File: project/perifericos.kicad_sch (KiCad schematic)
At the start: 67 parts, among them P1 Conector 2x10, P2 Conector 2x10, P3 Conector 2x10, P4 Conector 2x10, SW1 SW_Push, SW2 SW_Push, SW3 SW_Push, SW4 SW_Push, SW5 SW_Push, SW6 SW_Push, SW7 SW_Push, SW8 SW_Push, U6 ICE40HX4K-TQ144, Y2 ECS-3225MVQ-1000-CN-TR

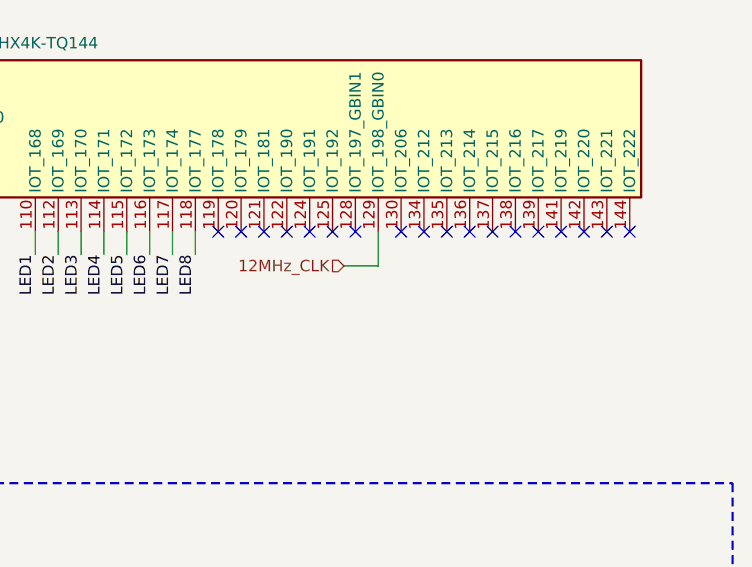
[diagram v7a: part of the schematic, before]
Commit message: Correciones de pistas varias, sacando una pista entre pads de la eeprom, ordenamiento de algunas vias, cambio de cristal de 12mhz al lado del ftdi, etc
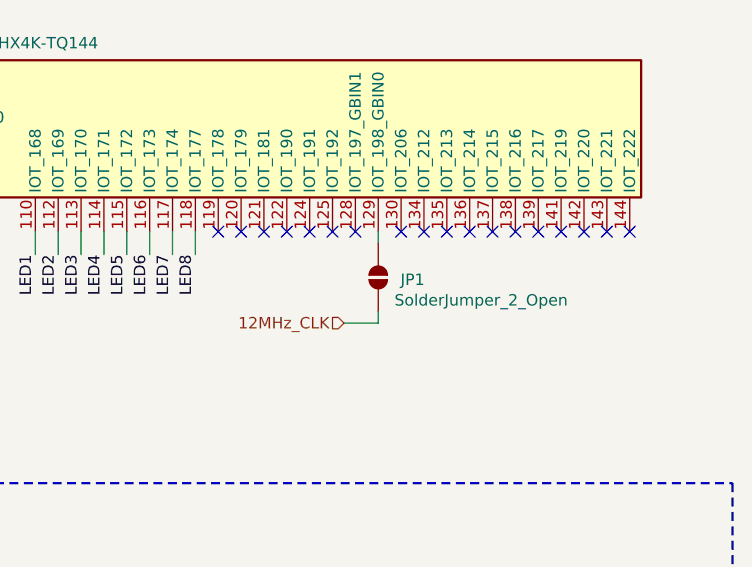
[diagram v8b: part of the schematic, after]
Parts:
- added JP1: SolderJumper_2_Open, Jumper:SolderJumper-2_P1.3mm_Open_TrianglePad1.0x1.5mm, symbol Jumper:SolderJumper_2_Open
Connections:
- net 12MHz_CLK: now also JP1.1 (A); no longer U6.129 (IOT_198_GBIN0)
- new net: JP1.2 (B), U6.129 (IOT_198_GBIN0)
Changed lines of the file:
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@@
 	(wire
 		(pts
+			(xy 242.57 55.88) (xy 242.57 54.61)
+		)
+		(stroke
+			(width 0)
+			(type default)
+		)
+	)
+	(wire
+		(pts
 			(xy 151.13 45.72) (xy 151.13 48.26)
 		)
@@
 	(wire
 		(pts
-			(xy 242.57 49.53) (xy 242.57 45.72)
-		)
-		(stroke
-			(width 0)
-			(type default)
-		)
-	)
-	(wire
-		(pts
 			(xy 187.96 95.25) (xy 187.96 96.52)
 		)
@@
 	(wire
 		(pts
-			(xy 238.76 49.53) (xy 242.57 49.53)
-		)
-		(stroke
-			(width 0)
-			(type default)
-		)
-	)
-	(wire
-		(pts
 			(xy 45.72 57.15) (xy 48.26 57.15)
 		)
@@
 	(wire
 		(pts
+			(xy 238.76 55.88) (xy 242.57 55.88)
+		)
+		(stroke
+			(width 0)
+			(type default)
+		)
+	)
+	(wire
+		(pts
 			(xy 92.71 187.96) (xy 95.25 187.96)
 		)
@@
 	(wire
 		(pts
+			(xy 242.57 45.72) (xy 242.57 46.99)
+		)
+		(stroke
+			(width 0)
+			(type default)
+		)
+	)
+	(wire
+		(pts
 			(xy 132.08 55.88) (xy 132.08 58.42)
 		)
@@
 	(hierarchical_label "12MHz_CLK"
 		(shape input)
-		(at 238.76 49.53 180)
+		(at 238.76 55.88 180)
 		(effects
 			(font
@@
 					(unit 1)
 				)
+			)
+		)
+	)
+	(symbol
+		(lib_id "Jumper:SolderJumper_2_Open")
+		(at 242.57 50.8 90)
+		(unit 1)
+		(exclude_from_sim no)
+		(in_bom no)
+		(on_board yes)
+		(dnp no)
+		(property "Reference" "JP1"
+			(at 246.38 51.054 90)
+			(effects
+				(font
+					(size 1.27 1.27)
+				)
+			)
+		)
+		(property "Value" "SolderJumper_2_Open"
+			(at 254 53.34 90)
+			(effects
+				(font
+					(size 1.27 1.27)
+				)
+			)
+		)
+		(property "Footprint" "Jumper:SolderJumper-2_P1.3mm_Open_TrianglePad1.0x1.5mm"
+			(at 242.57 50.8 0)
+			(effects
+				(font
+					(size 1.27 1.27)
+				)
+				(hide yes)
+			)
+		)
+		(property "Datasheet" "~"
+			(at 242.57 50.8 0)
+			(effects
+				(font
+					(size 1.27 1.27)
+				)
+				(hide yes)
+			)
+		)
+		(property "Description" "Solder Jumper, 2-pole, open"
+			(at 242.57 50.8 0)
+			(effects
+				(font
+					(size 1.27 1.27)
+				)
+				(hide yes)
+			)
+		)
+		(pin "2"
+		)
+		(pin "1"
+		)
+		(instances
+			(project ""
+				(path "/fadb8841-cd7a-4174-937d-7c393e857c90/4f5cf70b-0d7b-4ae8-aaf1-c3143c29443f"
+					(reference "JP1")
+					(unit 1)
+				)
